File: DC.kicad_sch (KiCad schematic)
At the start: 87 parts, among them J1 348302001, J2 348302001, J3 757570141, U6 MCP2551-I-P, U7 NUCLEO-F302R8

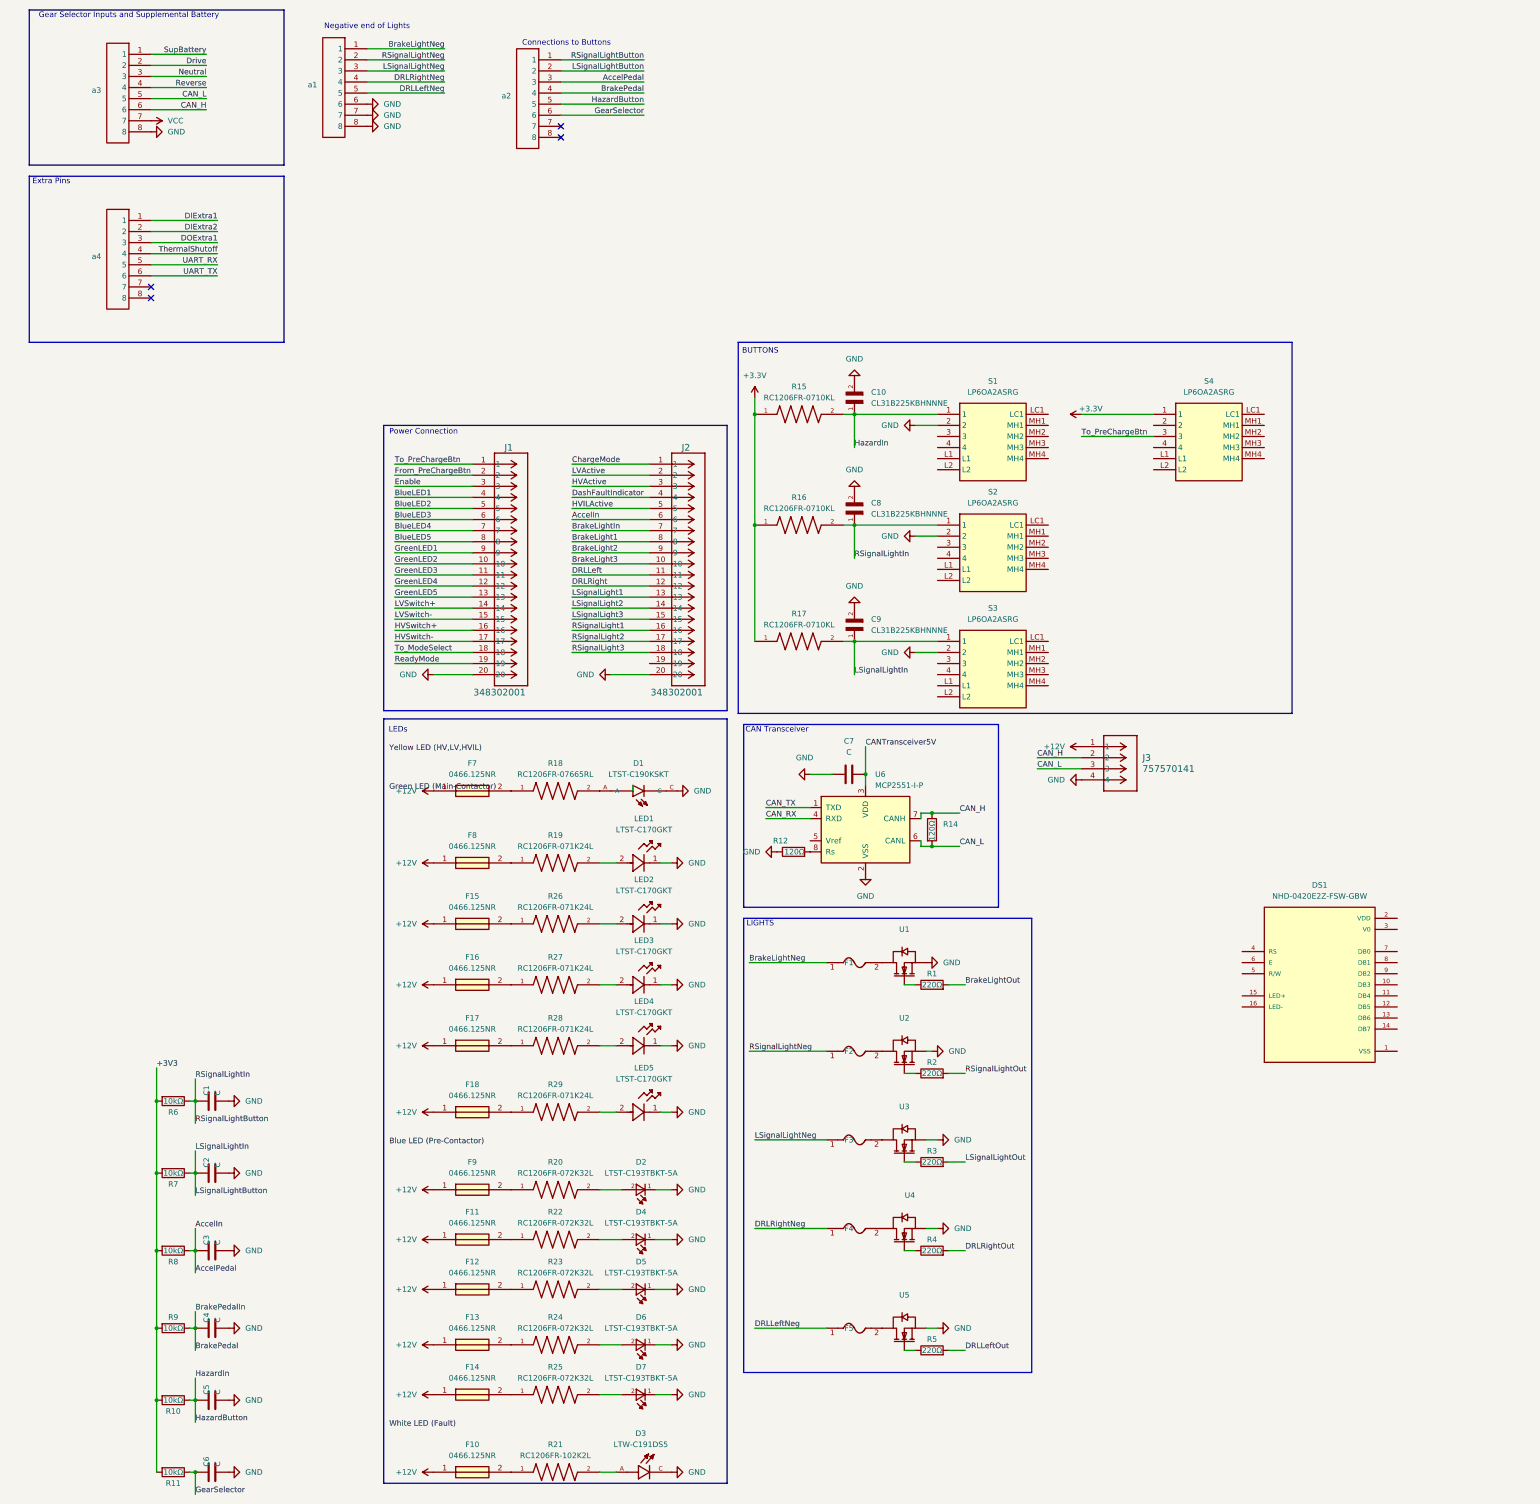
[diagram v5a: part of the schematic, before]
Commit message: Symbols all have a footprint and LCD added
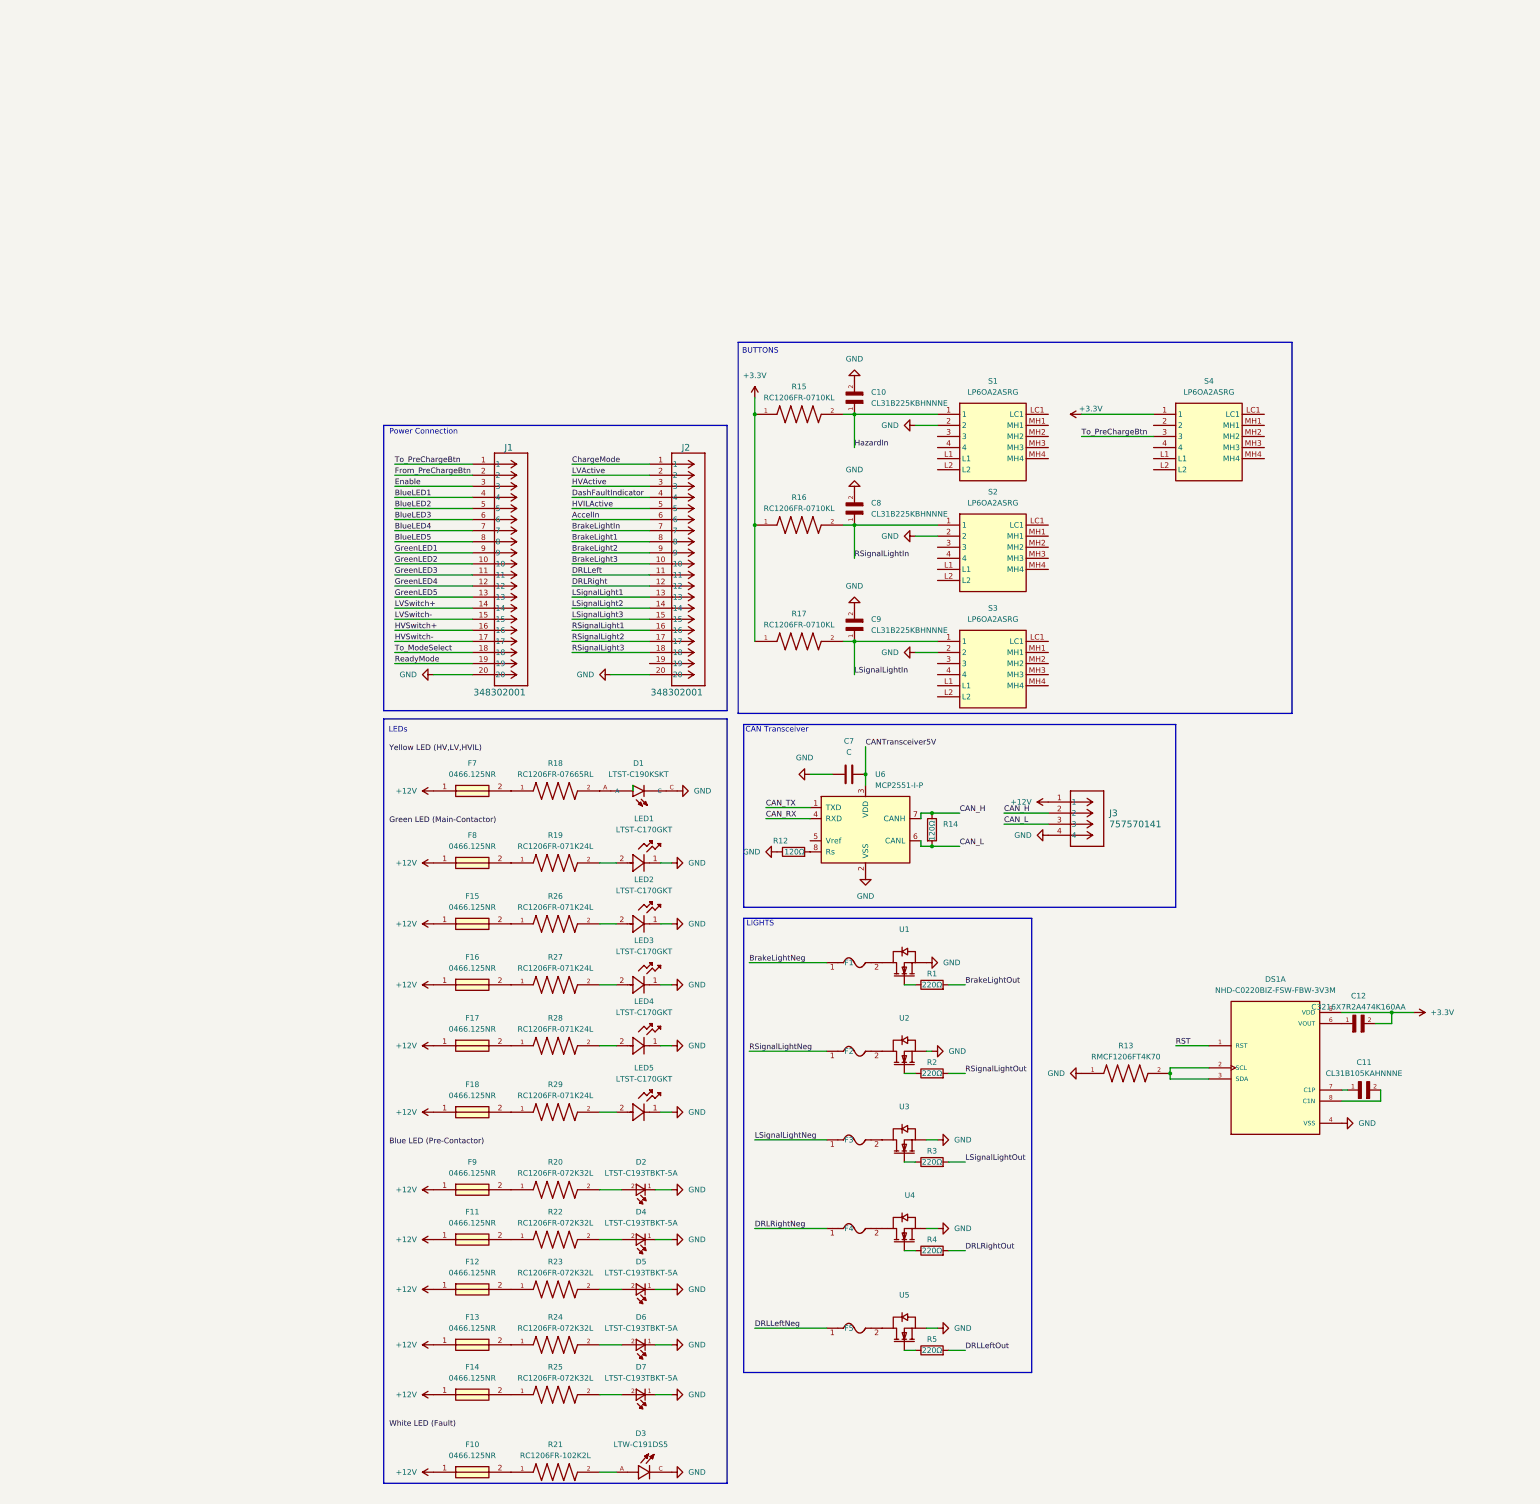
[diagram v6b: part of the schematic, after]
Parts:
- removed C1, C2, C3, C4, C5, C6: C, DriverControlsLib:CAP-TH_L6.0-W3.5-P7.50-D1.0, symbol DC_Parts:C
- removed DS1: NHD-0420E2Z-FSW-GBW, MiscellaneousLibrary:LCD_NHD-0420E2Z-FSW-GBW, symbol NHD-0420E2Z-FSW-GBW:NHD-0420E2Z-FSW-GBW
- removed R10, R11, R6, R7, R8, R9: 10kΩ, DriverControlsLib:RES-TH_BD2.2-L6.5-P10.50-D0.6, symbol DC_Parts:R
- removed a1, a2, a3, a4: ~, DriverControlsLib:Molex 8 Pin Mini-fit TPA, symbol DC_Parts:8 pin connector
- added C11: CL31B105KAHNNNE, Capacitor_SMD:CAPC3216X180N, symbol CL31B105KAHNNNE:CL31B105KAHNNNE
- added C12: C3216X7R2A474K160AA, Capacitor_SMD:CAPC3216X180N, symbol C3216X7R2A474K160AA:C3216X7R2A474K160AA
- added DS1: NHD-C0220BIZ-FSW-FBW-3V3M, Display:LCD_NHD-C0220BIZ-FSW-FBW-3V3M, symbol NHD-C0220BIZ-FSW-FBW-3V3M:NHD-C0220BIZ-FSW-FBW-3V3M
- added R13: RMCF1206FT4K70, Resistor_SMD:RESC3216X70N, symbol RMCF1206FT4K70:RMCF1206FT4K70
- C10, C8, C9: footprint CL31B225KBHNNNE:CAPC3216X180N -> Capacitor_SMD:CAPC3216X180N
- D1: footprint LTST-C190KSKT:LEDM1608X80 -> LED_SMD:LEDM1608X80
- D2, D4, D5, D6, D7: footprint LTST-C193TBKT-5A:0603 -> Fuse:Fuse_0603_1608Metric
- F10, F11, F12, F13, F14, F15, F16, F17, F18, F7, F8, F9: footprint (none) -> Fuse:FUSC3215X66N
- J1, J2: footprint (none) -> Connector_Molex:CONN_SD-34829-001_20_ST_MOL
- J3: footprint (none) -> Connector_Molex:CONN_SD-75757-010_1X4_F11p20_MOL
- LED1, LED2, LED3, LED4, LED5: footprint (none) -> LED_SMD:LED_LTST-C170GKT_LTO
- R15, R16, R17: footprint RC1206FR-0710KL:RESC3116X65N -> Resistor_SMD:RESC3116X65N
- R18: footprint RC1206FR-07665RL:RESC3116X65N -> Resistor_SMD:RESC3116X65N
- R19, R26, R27, R28, R29: footprint RC1206FR-071K24L:RESC3116X65N -> Resistor_SMD:RESC3116X65N
- R20, R22, R23, R24, R25: footprint RC1206FR-072K32L:RESC3116X65N -> Resistor_SMD:RESC3116X65N
- R21: footprint RC1206FR-102K2L:RESC3116X65N -> Resistor_SMD:RESC3116X65N
- S1, S2, S3, S4: footprint (none) -> Button_Switch_SMD:LP6OA2ASRG
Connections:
- net +3.3V: now also C12.2, DS1.5 (VDD)
- net GND: now also DS1.4 (VSS), R13.1
- net BrakePedal renamed BrakePedalIn
- net HazardButton renamed HazardIn
- net LSignalLightButton renamed LSignalLightIn
- net RSignalLightButton renamed RSignalLightIn
- new net: DS1.2 (SCL), DS1.3 (SDA), R13.2
- new net: C12.1, DS1.6 (VOUT)
- new net: C11.1, DS1.7 (C1P)
- new net: C11.2, DS1.8 (C1N)
- new net RST: DS1.1 (RST)
- no-connect marks 39 -> 35
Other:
- note removed: "Connections to Buttons"
- note removed: "Extra Pins"
- note removed: "Gear Selector Inputs and Supplemental Battery"
- note removed: "Negative end of Lights"
- moved on the sheet: J3

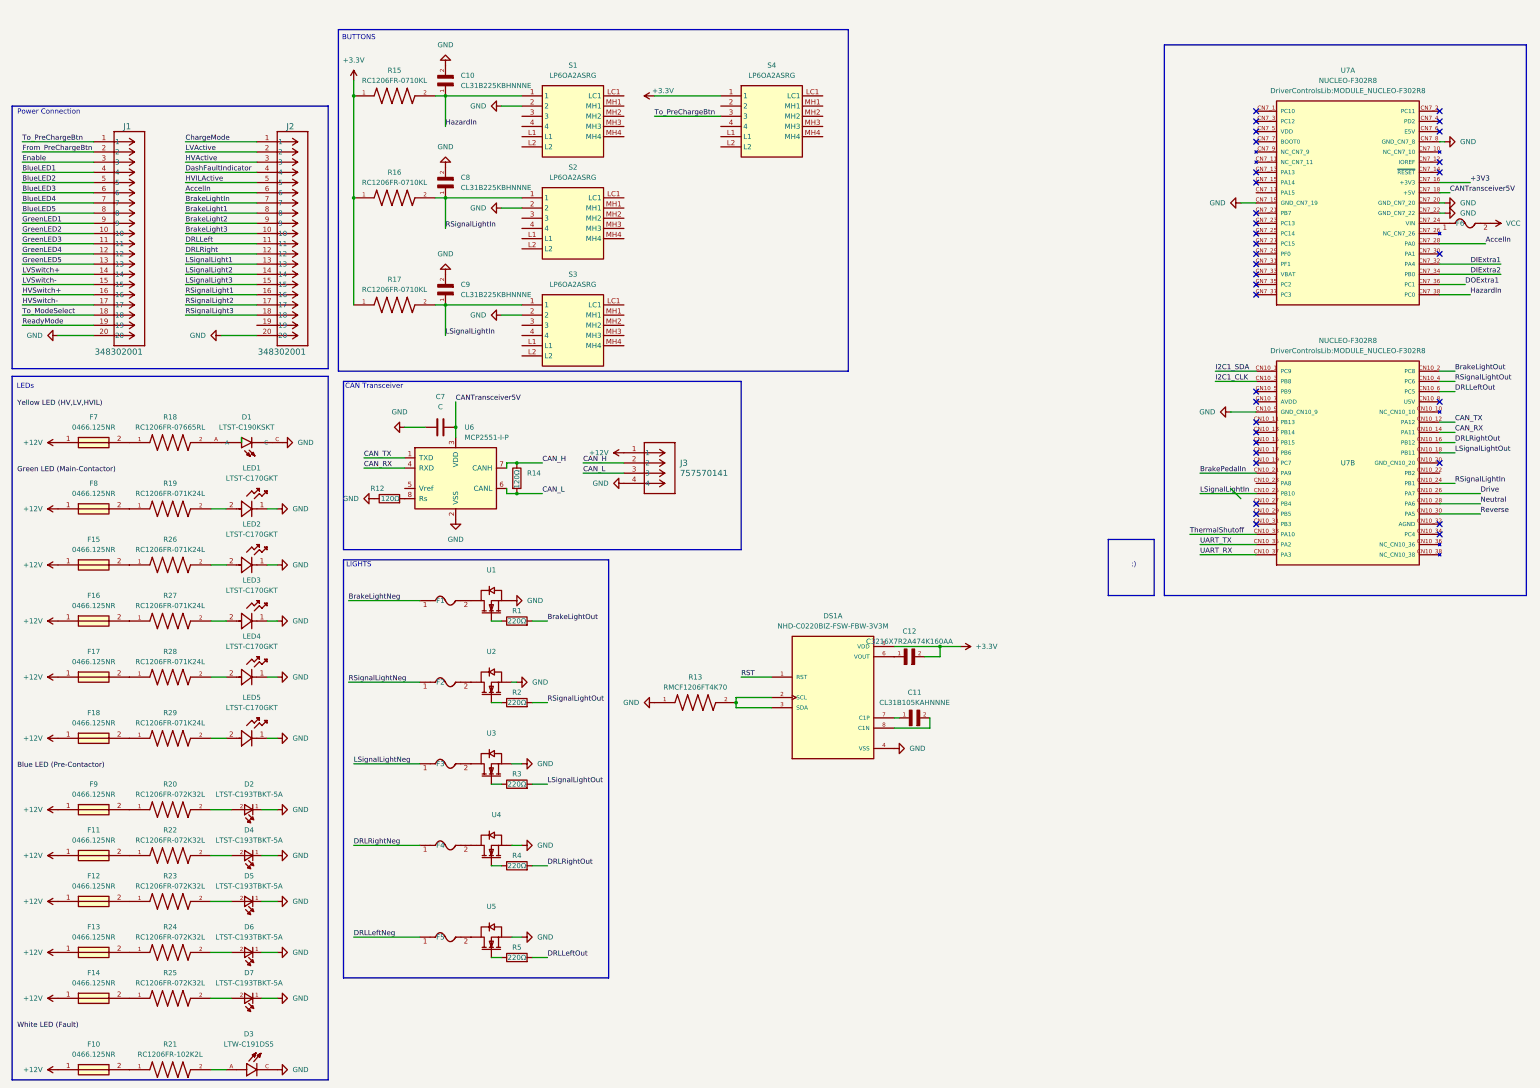
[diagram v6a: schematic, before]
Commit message: Fixed airwires and CANtransceiver, added mode select switch
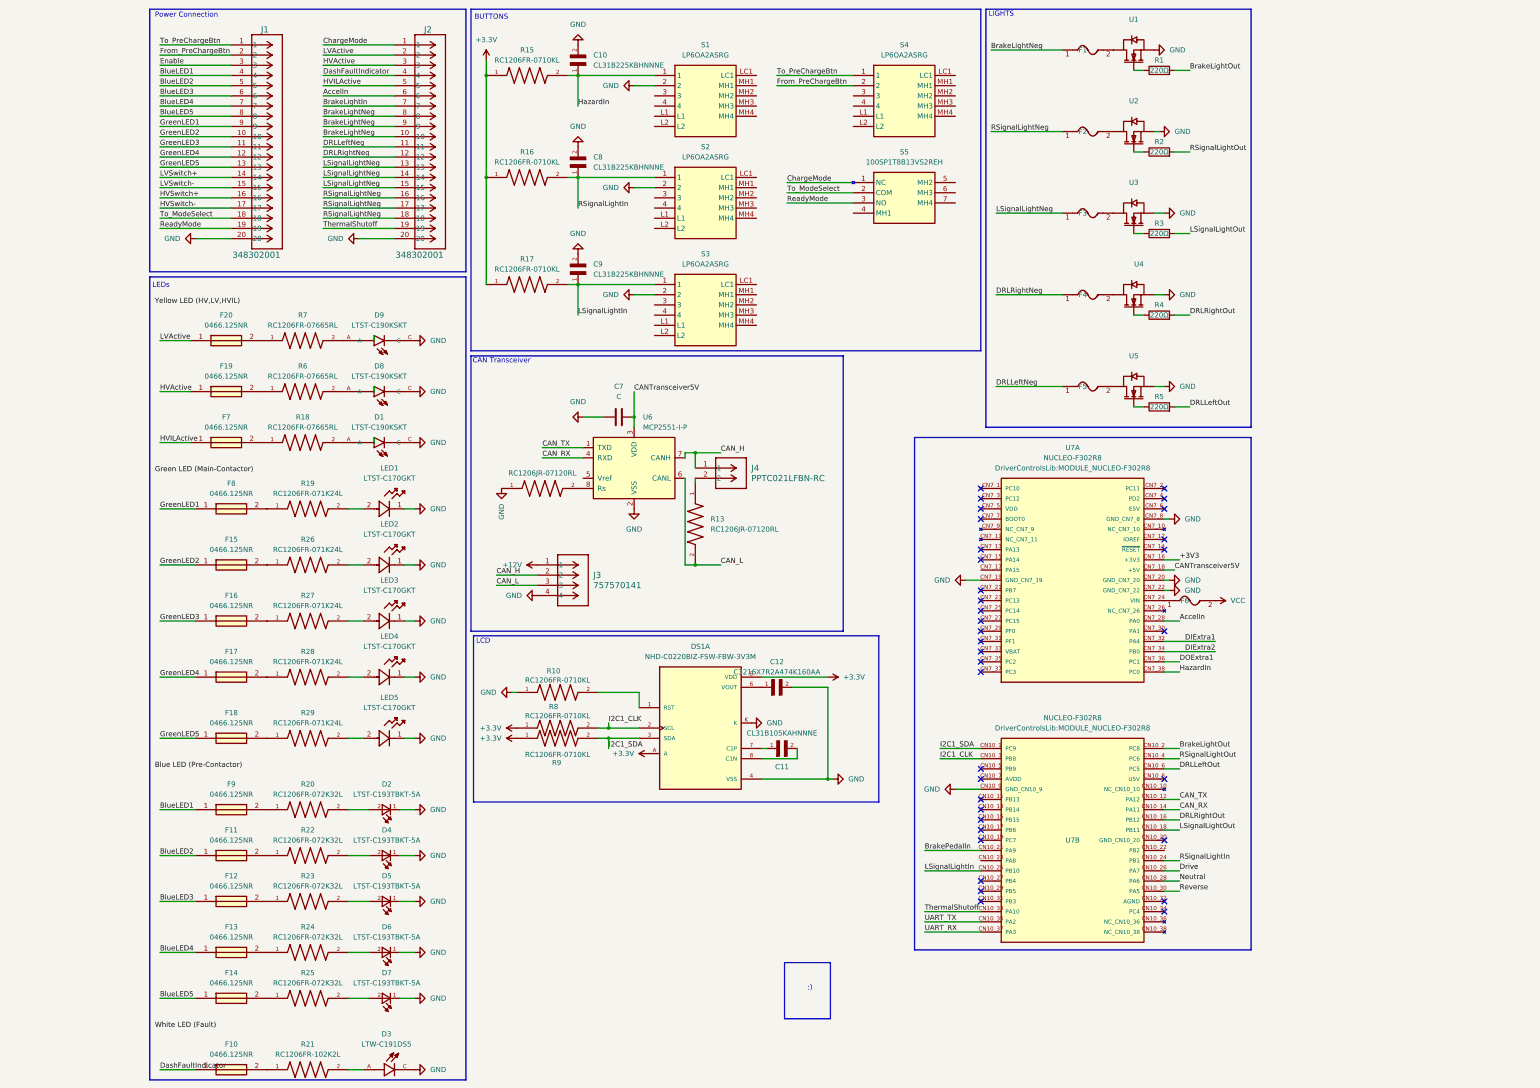
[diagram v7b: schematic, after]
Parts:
- removed R12, R14: 120Ω, DriverControlsLib:RES-TH_BD2.2-L6.5-P10.50-D0.6, symbol DC_Parts:R
- removed R13: RMCF1206FT4K70, Resistor_SMD:RESC3216X70N, symbol RMCF1206FT4K70:RMCF1206FT4K70
- added D8, D9: LTST-C190KSKT, LED_SMD:LEDM1608X80, symbol LTST-C190KSKT:LTST-C190KSKT
- added F19, F20: 0466.125NR, Fuse:FUSC3215X66N, symbol 0466_125NR:0466.125NR
- added J4: PPTC021LFBN-RC, Connector:CONN2_LFBN-RC_SUL, symbol 2026-02-13_01-22-03:PPTC021LFBN-RC
- added R10, R8, R9: RC1206FR-0710KL, Resistor_SMD:RESC3116X65N, symbol RC1206FR-0710KL:RC1206FR-0710KL
- added R11, R13: RC1206JR-07120RL, Resistor_SMD:RESC3116X65N, symbol RC1206JR-07120RL:RC1206JR-07120RL
- added R6, R7: RC1206FR-07665RL, Resistor_SMD:RESC3116X65N, symbol RC1206FR-07665RL:RC1206FR-07665RL
- added S5: 100SP1T8B13VS2REH, Button_Switch_SMD:100SP1T8B13VS2REH, symbol 100SP1T8B13VS2REH:100SP1T8B13VS2REH
- D3: footprint LTW-C191DS5:LEDC1608X65N -> LED_SMD:LEDC1608X65N
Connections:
- net BrakeLight1 is gone; now on net BrakeLightNeg: J2.8
- net BrakeLight2 is gone; now on net BrakeLightNeg: J2.9
- net BrakeLight3 is gone; now on net BrakeLightNeg: J2.10
- net DRLLeft is gone; now on net DRLLeftNeg: J2.11
- net DRLRight is gone; now on net DRLRightNeg: J2.12
- net LSignalLight1 is gone; now on net LSignalLightNeg: J2.13
- net LSignalLight2 is gone; now on net LSignalLightNeg: J2.14
- net LSignalLight3 is gone; now on net LSignalLightNeg: J2.15
- net RSignalLight1 is gone; now on net RSignalLightNeg: J2.16
- net RSignalLight2 is gone; now on net RSignalLightNeg: J2.17
- net RSignalLight3 is gone; now on net RSignalLightNeg: J2.18
- net +12V: no longer F10.1, F11.1, F12.1, F13.1, F14.1, F15.1, F16.1, F17.1, F18.1, F7.1, F8.1, F9.1
- net +3.3V: now also DS1.A, R8.1, R9.1; no longer C12.2, S4.1
- net BlueLED1: now also F9.1
- net BlueLED2: now also F11.1
- net BlueLED3: now also F12.1
- net BlueLED4: now also F13.1
- net BlueLED5: now also F14.1
- net CAN_H: now also J4.1
- net CAN_L: now also R13.2
- net ChargeMode: now also S5.1 (NC)
- net DashFaultIndicator: now also F10.1
- net From_PreChargeBtn: now also S4.2
- net GND: now also C12.2, DS1.K, D8.C, D9.C, R10.1, R11.1
- net GreenLED1: now also F8.1
- net GreenLED2: now also F15.1
- net GreenLED3: now also F16.1
- net GreenLED4: now also F17.1
- net GreenLED5: now also F18.1
- net HVActive: now also F19.1
- net HVILActive: now also F7.1
- net I2C1_CLK: now also DS1.2 (SCL), R8.2
- net I2C1_SDA: now also DS1.3 (SDA), R9.2
- net LVActive: now also F20.1
- net ReadyMode: now also S5.3 (NO)
- net ThermalShutoff: now also J2.19
- net To_ModeSelect: now also S5.2 (COM)
- net To_PreChargeBtn: now also S4.1; no longer S4.3
- net at U6.8 (Rs): now also R11.2
- net RST: no longer names the net of DS1.1 (RST)
- net RST: now also R10.2
- new net: D8.A, R6.2
- new net: J4.2, R13.1
- new net: F19.2, R6.1
- new net: D9.A, R7.2
- new net: F20.2, R7.1
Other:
- note added: "LCD"
- moved on the sheet: C10, C11, C12, C7, C8, C9, D1, D2, D3, D4, D5, D6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
